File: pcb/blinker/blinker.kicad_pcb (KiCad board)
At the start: 2 copper layers, 68 x 76 mm, 14 parts, among them J1 Conn_01x04_Pin, J2 Conn_01x02_Pin_for_flashing, J3 Screw_Terminal_01x04, Q1 BC547, SW2 SW_MEC_5E, U1 ESP-12F

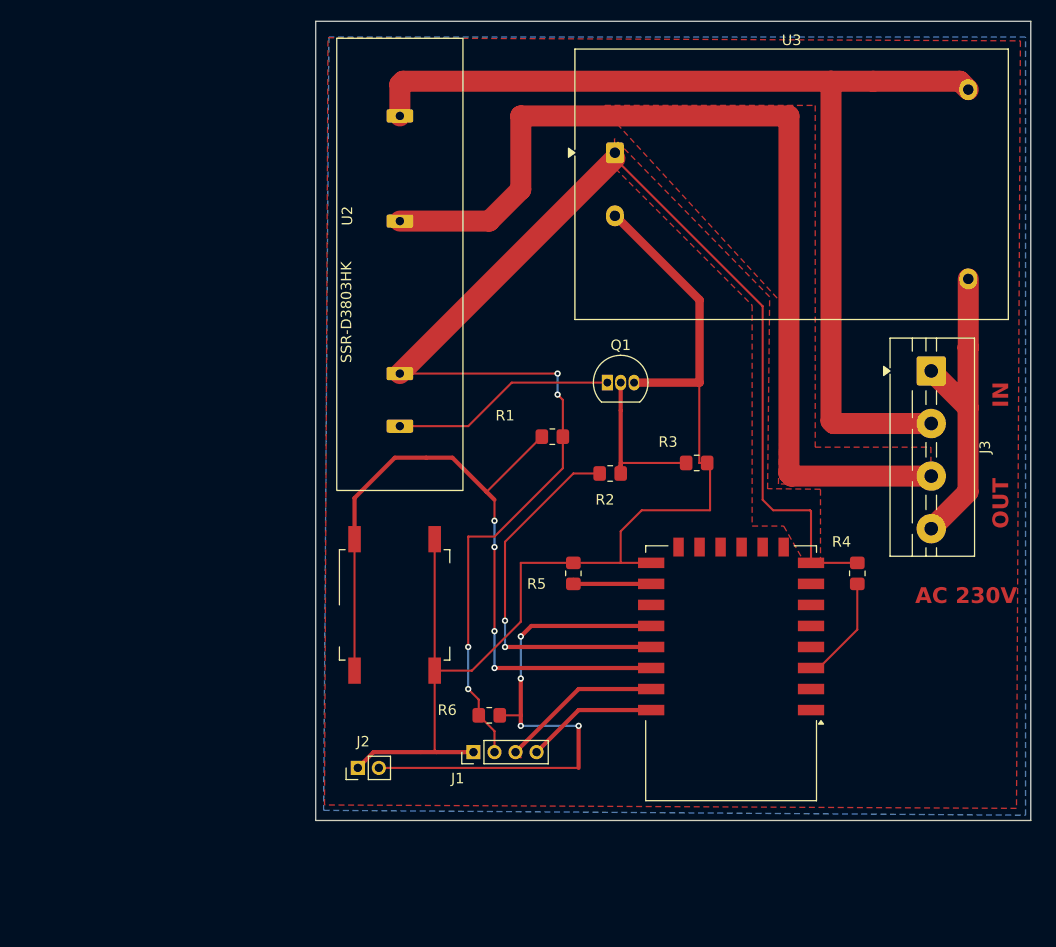
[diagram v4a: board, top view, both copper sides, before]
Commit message: Put PCB resistor in one line
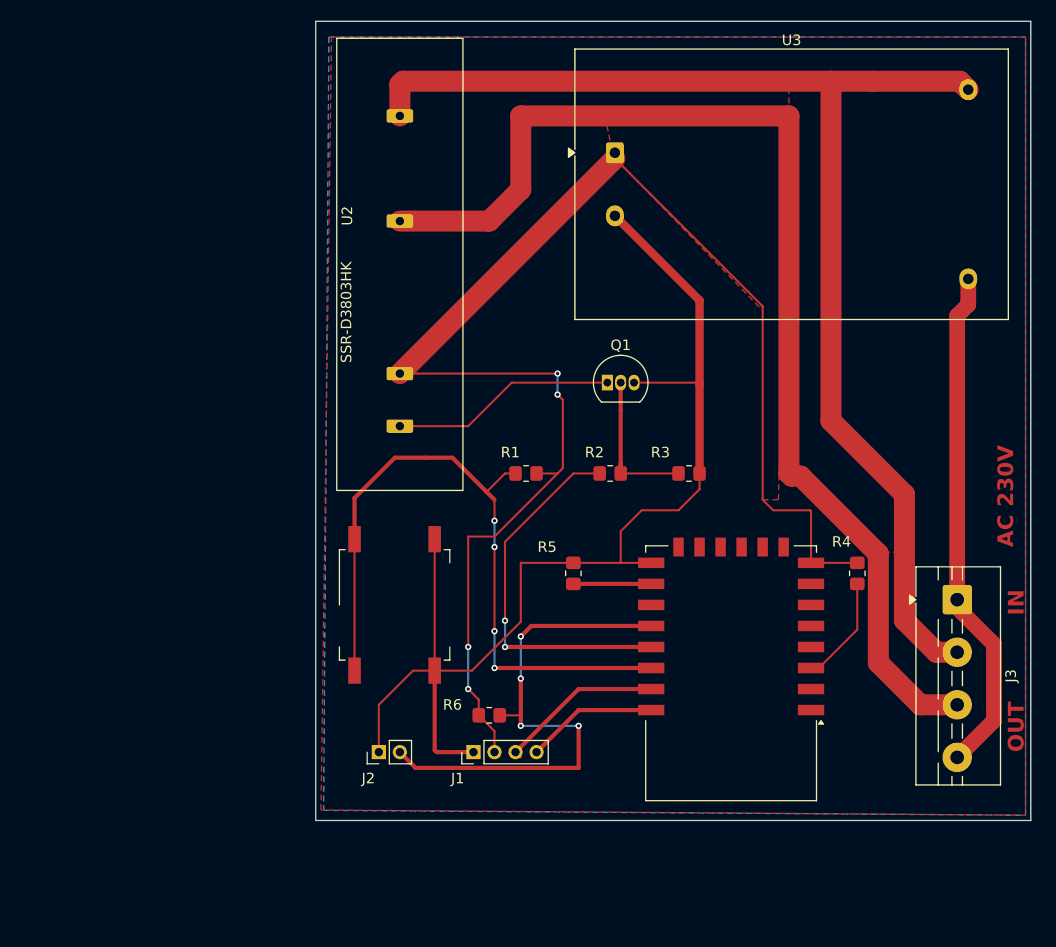
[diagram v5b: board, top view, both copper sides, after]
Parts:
- moved J3 21.9 mm to (146.5, 82.5)
- moved R1 4.30 mm to (105.5, 70.5)
- moved J2 2.50 mm to (91.5, 97.0)
- moved R3 1.24 mm to (121.0, 70.5)
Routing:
- net Net-(J3-Pin_2): track 99.4 -> 117.9 mm
- net Net-(J3-Pin_1): track 30.2 -> 48.1 mm
- net Net-(J3-Pin_3): track 92.9 -> 110.4 mm
- net Net-(U1-GPIO5): track 71.3 -> 67.3 mm
- net +3.3V: track 140.2 -> 142.2 mm
- net Net-(J2-Pin_2): track 51.8 -> 50.4 mm
- net Net-(Q1-B): track 14.6 -> 13.8 mm
- added copper zone on F.Cu, net Net-(J3-Pin_2)
- removed copper zone on F.Cu, net Net-(J3-Pin_3)

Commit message: Change to Converter_ACDC:HLK-5M03
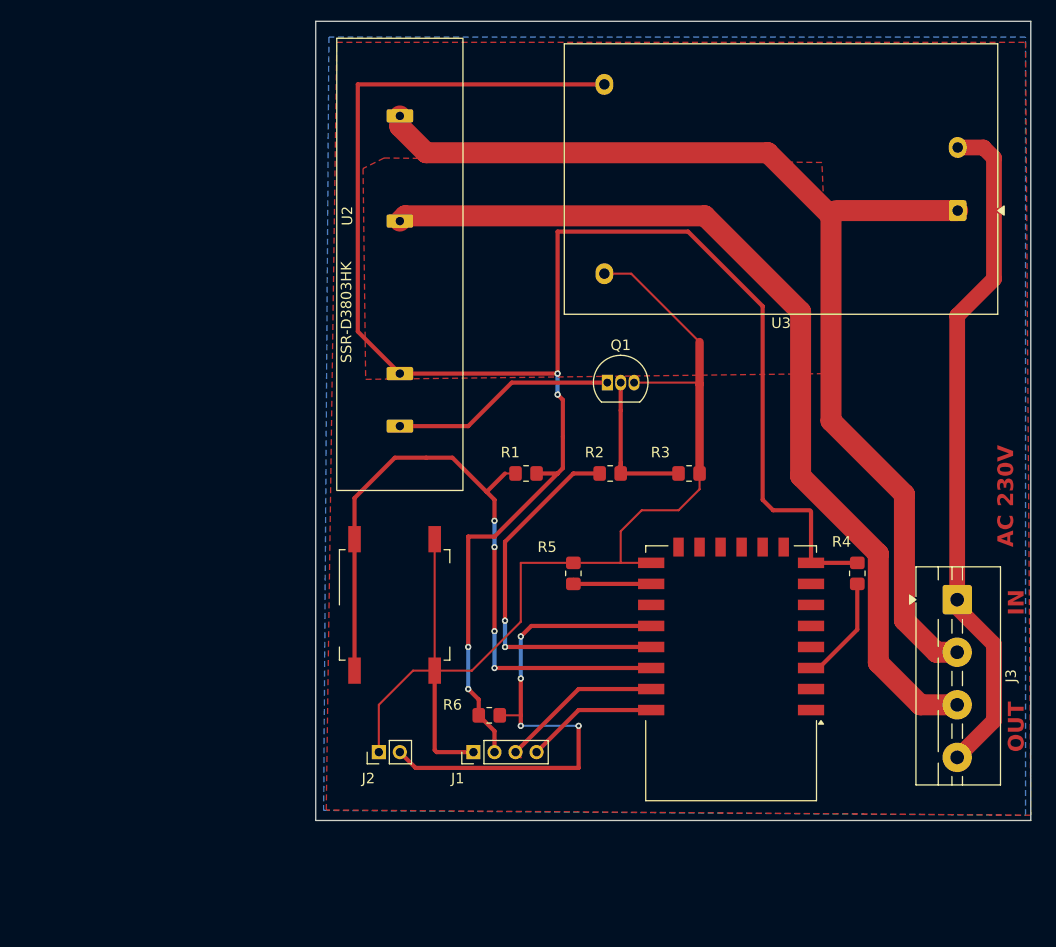
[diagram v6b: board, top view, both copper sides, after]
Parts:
- U3: value ~ -> HLK-5M03
- moved U3 33.1 mm to (146.5, 45.5), turned to 180 degrees
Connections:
- U3 pad 1: +3.3V -> Net-(J3-Pin_2)
- U3 pad 2: GND -> Net-(J3-Pin_1)
- U3 pad 3: Net-(J3-Pin_2) -> GND
- U3 pad 4: Net-(J3-Pin_1) -> +3.3V
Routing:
- net +3.3V: track 142.2 -> 180.7 mm
- net Net-(J3-Pin_3): track 110.4 -> 87.7 mm
- net Net-(J3-Pin_1): track 48.1 -> 64.5 mm
- net Net-(J3-Pin_2): track 117.9 -> 105.4 mm
- net GND: track 110.6 -> 107.0 mm
- removed copper zone on F.Cu, net Net-(J3-Pin_2)

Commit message: Add image
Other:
- board text added: "3V3"
- board text added: "GND"
- board text added: "RXD"
- board text added: "TXD"
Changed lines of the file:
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@@
 		(tags "Through hole pin header THT 1x04 2.00mm single row")
 		(property "Reference" "J1"
-			(at -2.5 -1.5 180)
+			(at -2.5 -2 180)
 			(layer "F.SilkS")
 			(effects
@@
 		(layer "Edge.Cuts")
 	)
+	(gr_text "GND"
+		(at 99.5 99.5 0)
+		(layer "F.Cu")
+		(effects
+			(font
+				(size 0.5 0.5)
+				(thickness 0.125)
+				(bold yes)
+			)
+			(justify left bottom)
+		)
+	)
+	(gr_text "3V3"
+		(at 101.5 99.5 0)
+		(layer "F.Cu")
+		(effects
+			(font
+				(size 0.5 0.5)
+				(thickness 0.125)
+				(bold yes)
+			)
+			(justify left bottom)
+		)
+	)
+	(gr_text "RXD"
+		(at 103.5 99.5 0)
+		(layer "F.Cu")
+		(effects
+			(font
+				(size 0.5 0.5)
+				(thickness 0.125)
+				(bold yes)
+			)
+			(justify left bottom)
+		)
+	)
+	(gr_text "TXD"
+		(at 106 99.5 0)
+		(layer "F.Cu")
+		(effects
+			(font
+				(size 0.5 0.5)
+				(thickness 0.125)
+				(bold yes)
+			)
+			(justify left bottom)
+		)
+	)
 	(gr_text "AC 230V"
 		(at 152 77.5 90)
@@
 			)
 			(justify left bottom)
+		)
+	)
+	(gr_text "GND"
+		(at 99.5 99.5 0)
+		(layer "F.SilkS")
+		(effects
+			(font
+				(size 0.5 0.5)
+				(thickness 0.125)
+				(bold yes)
+			)
+			(justify left bottom)
+		)
+	)
+	(gr_text "3V3"
+		(at 101.5 99.5 0)
+		(layer "F.SilkS")
+		(effects
+			(font
+				(size 0.5 0.5)
+				(thickness 0.125)
+				(bold yes)
+			)
+			(justify left bottom)
+		)
+	)
+	(gr_text "RXD"
+		(at 103.5 99.5 0)
+		(layer "F.SilkS")
+		(effects
+			(font
+				(size 0.5 0.5)
+				(thickness 0.125)
+				(bold yes)
+			)
+			(justify left bottom)
+		)
+	)
+	(gr_text "TXD"
+		(at 106 99.5 0)
+		(layer "F.SilkS")
+		(effects
+			(font
+				(size 0.5 0.5)
+				(thickness 0.125)
+				(bold yes)
+			)
+			(justify left bottom)
